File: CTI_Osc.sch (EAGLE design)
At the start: 15 parts, among them IC6 7805DT

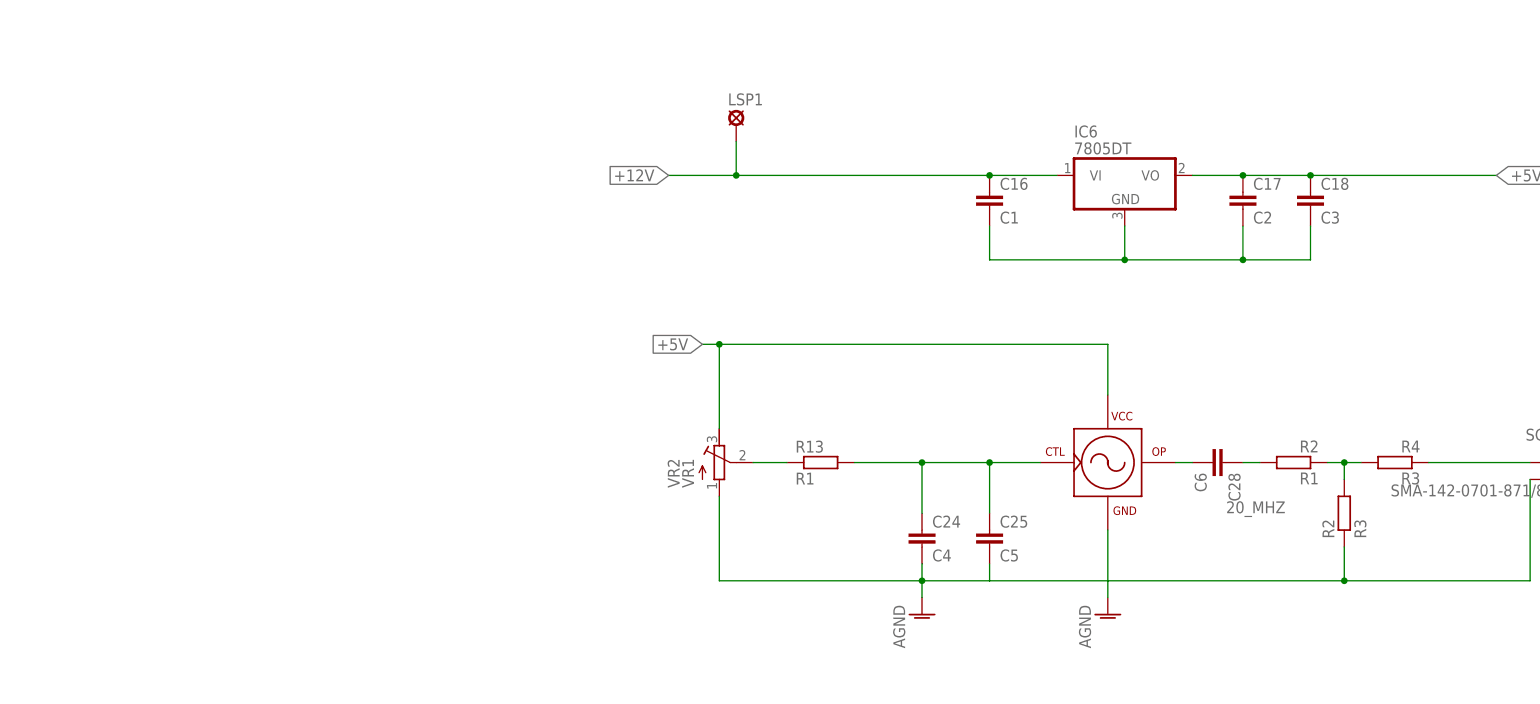
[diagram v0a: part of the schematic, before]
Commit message: V1 release
Added a TL431C for precision control of the freq set pin.
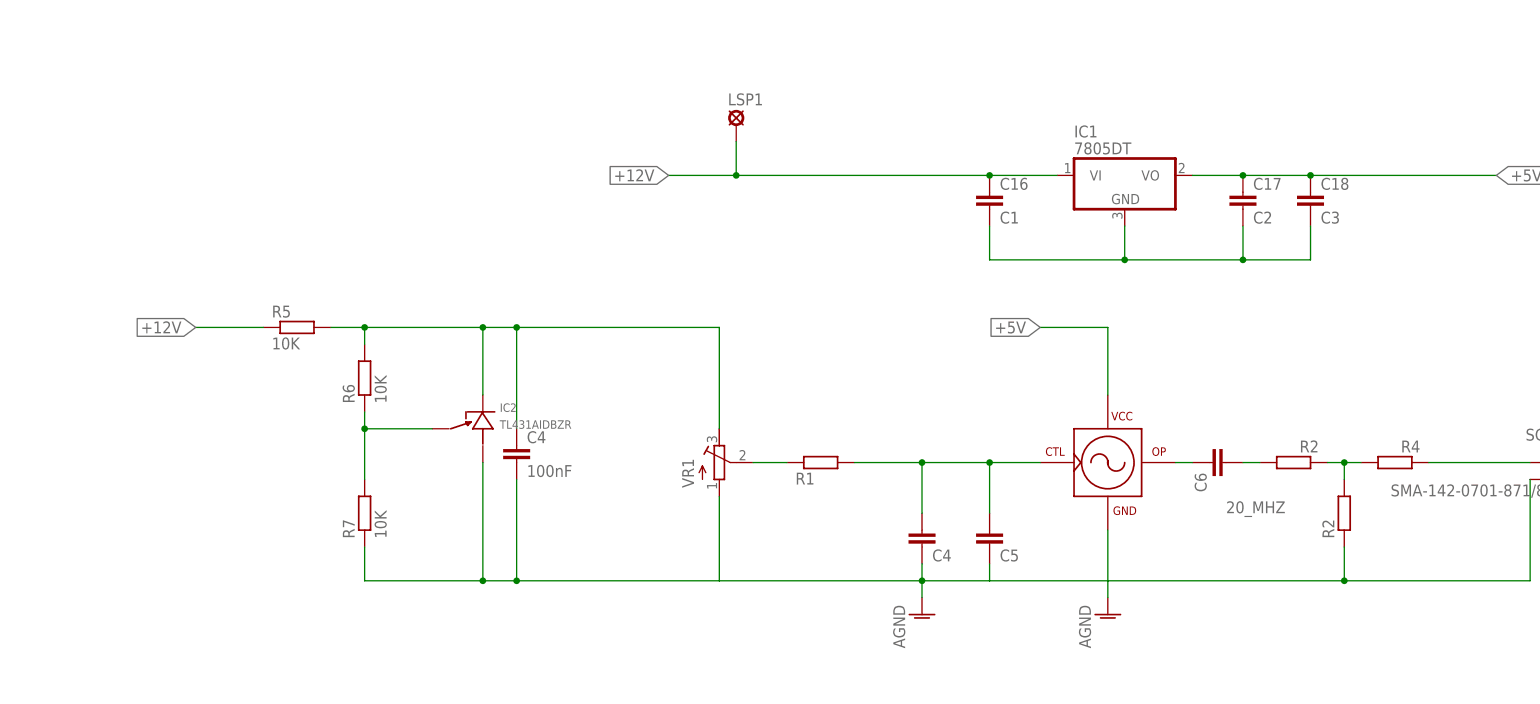
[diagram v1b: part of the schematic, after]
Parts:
- added C4: 100nF, rcl:C-EUC0603
- added IC2: TL431AIDBZR, RF:TL431AIDBZR
- added R5, R6, R7: 10K, rcl:R-EU_R0603
- renumbered IC6 to IC1
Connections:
- new net +5V_PRECISION: C4.1, IC2.CATHODE, R5.2, R6.2, VR2.A
- new net N$42: IC2.CTRL, R6.1, R7.2
- net +12V: now also R5.1
- net +5V: no longer VR2.A
- net GND: now also C4.2, IC2.ANODE, R7.1
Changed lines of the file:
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@@
 <part name="SCK1" library="con-coax" deviceset="SMA-" device="142-0701-871/876"/>
 <part name="OSC1" library="RF" deviceset="CTI_OSC" device=""/>
-<part name="IC6" library="linear" deviceset="78*" device="DT" technology="05" value="7805DT"/>
+<part name="IC1" library="linear" deviceset="78*" device="DT" technology="05" value="7805DT"/>
 <part name="C16" library="rcl" deviceset="C-EU" device="C0805" value="C1"/>
 <part name="C17" library="rcl" deviceset="C-EU" device="C0805" value="C2"/>
@@
 <part name="R1" library="rcl" deviceset="R-EU_" device="R0603" value="R2"/>
 <part name="VR2" library="resistor" deviceset="R-TRIMM" device="64Y" value="VR1"/>
+<part name="IC2" library="RF" deviceset="TL431AIDBZR" device=""/>
+<part name="R5" library="rcl" deviceset="R-EU_" device="R0603" value="10K"/>
+<part name="R7" library="rcl" deviceset="R-EU_" device="R0603" value="10K"/>
+<part name="R6" library="rcl" deviceset="R-EU_" device="R0603" value="10K"/>
+<part name="C4" library="rcl" deviceset="C-EU" device="C0603" value="100nF"/>
 </parts>
 <sheets>
@@
 <instance part="U$5" gate="CCSA" x="515.62" y="0"/>
 <instance part="AGND39" gate="VR1" x="175.26" y="152.4"/>
-<instance part="C24" gate="G$1" x="147.32" y="165.1"/>
+<instance part="C24" gate="G$1" x="147.32" y="165.1" smashed="yes">
+<attribute name="VALUE" x="148.844" y="160.401" size="1.778" layer="96"/>
+</instance>
 <instance part="AGND40" gate="VR1" x="147.32" y="152.4"/>
-<instance part="C25" gate="G$1" x="157.48" y="165.1"/>
-<instance part="R13" gate="G$1" x="132.08" y="175.26"/>
-<instance part="C28" gate="G$1" x="193.04" y="175.26" rot="R270"/>
+<instance part="C25" gate="G$1" x="157.48" y="165.1" smashed="yes">
+<attribute name="VALUE" x="159.004" y="160.401" size="1.778" layer="96"/>
+</instance>
+<instance part="R13" gate="G$1" x="132.08" y="175.26" smashed="yes">
+<attribute name="VALUE" x="128.27" y="171.958" size="1.778" layer="96"/>
+</instance>
+<instance part="C28" gate="G$1" x="193.04" y="175.26" smashed="yes" rot="R270">
+<attribute name="VALUE" x="188.341" y="173.736" size="1.778" layer="96" rot="R270"/>
+</instance>
 <instance part="SCK1" gate="G1" x="241.3" y="175.26" rot="MR0"/>
 <instance part="OSC1" gate="G$1" x="170.18" y="170.18"/>
-<instance part="IC6" gate="A1" x="177.8" y="218.44"/>
+<instance part="IC1" gate="A1" x="177.8" y="218.44"/>
 <instance part="C16" gate="G$1" x="157.48" y="215.9"/>
 <instance part="C17" gate="G$1" x="195.58" y="215.9"/>
 <instance part="C18" gate="G$1" x="205.74" y="215.9"/>
 <instance part="LSP1" gate="1" x="119.38" y="226.06"/>
-<instance part="R2" gate="G$1" x="210.82" y="167.64" rot="R90"/>
-<instance part="R3" gate="G$1" x="218.44" y="175.26" rot="R180"/>
-<instance part="R1" gate="G$1" x="203.2" y="175.26" rot="R180"/>
-<instance part="VR2" gate="G$1" x="116.84" y="175.26"/>
+<instance part="R2" gate="G$1" x="210.82" y="167.64" smashed="yes" rot="R90">
+<attribute name="NAME" x="209.3214" y="163.83" size="1.778" layer="95" rot="R90"/>
+</instance>
+<instance part="R3" gate="G$1" x="218.44" y="175.26" smashed="yes" rot="R180">
+<attribute name="VALUE" x="222.25" y="178.562" size="1.778" layer="96" rot="R180"/>
+</instance>
+<instance part="R1" gate="G$1" x="203.2" y="175.26" smashed="yes" rot="R180">
+<attribute name="VALUE" x="207.01" y="178.562" size="1.778" layer="96" rot="R180"/>
+</instance>
+<instance part="VR2" gate="G$1" x="116.84" y="175.26" smashed="yes">
+<attribute name="VALUE" x="113.03" y="171.45" size="1.778" layer="96" rot="R90"/>
+</instance>
+<instance part="IC2" gate="G$1" x="81.28" y="180.34"/>
+<instance part="R5" gate="G$1" x="53.34" y="195.58"/>
+<instance part="R7" gate="G$1" x="63.5" y="167.64" rot="R90"/>
+<instance part="R6" gate="G$1" x="63.5" y="187.96" rot="R90"/>
+<instance part="C4" gate="G$1" x="86.36" y="177.8"/>
 </instances>
 <busses>
@@
 <pinref part="C16" gate="G$1" pin="2"/>
 <wire x1="157.48" y1="210.82" x2="157.48" y2="205.74" width="0.1524" layer="91"/>
-<pinref part="IC6" gate="A1" pin="GND"/>
+<pinref part="IC1" gate="A1" pin="GND"/>
 <wire x1="157.48" y1="205.74" x2="177.8" y2="205.74" width="0.1524" layer="91"/>
 <wire x1="177.8" y1="205.74" x2="177.8" y2="210.82" width="0.1524" layer="91"/>
@@
 <junction x="210.82" y="157.48"/>
 <pinref part="VR2" gate="G$1" pin="E"/>
+<pinref part="IC2" gate="G$1" pin="ANODE"/>
+<wire x1="81.28" y1="175.26" x2="81.28" y2="157.48" width="0.1524" layer="91"/>
+<wire x1="81.28" y1="157.48" x2="86.36" y2="157.48" width="0.1524" layer="91"/>
+<pinref part="R7" gate="G$1" pin="1"/>
+<wire x1="86.36" y1="157.48" x2="116.84" y2="157.48" width="0.1524" layer="91"/>
+<wire x1="63.5" y1="162.56" x2="63.5" y2="157.48" width="0.1524" layer="91"/>
+<wire x1="63.5" y1="157.48" x2="81.28" y2="157.48" width="0.1524" layer="91"/>
+<junction x="81.28" y="157.48"/>
+<pinref part="C4" gate="G$1" pin="2"/>
+<wire x1="86.36" y1="172.72" x2="86.36" y2="157.48" width="0.1524" layer="91"/>
+<junction x="86.36" y="157.48"/>
 </segment>
 </net>
@@
 <wire x1="119.38" y1="218.44" x2="109.22" y2="218.44" width="0.1524" layer="91"/>
 <pinref part="C16" gate="G$1" pin="1"/>
-<pinref part="IC6" gate="A1" pin="VI"/>
+<pinref part="IC1" gate="A1" pin="VI"/>
 <wire x1="157.48" y1="218.44" x2="167.64" y2="218.44" width="0.1524" layer="91"/>
 <junction x="157.48" y="218.44"/>
@@
 <wire x1="119.38" y1="223.52" x2="119.38" y2="218.44" width="0.1524" layer="91"/>
 <junction x="119.38" y="218.44"/>
+</segment>
+<segment>
+<pinref part="R5" gate="G$1" pin="1"/>
+<wire x1="48.26" y1="195.58" x2="38.1" y2="195.58" width="0.1524" layer="91"/>
+<label x="38.1" y="195.58" size="1.778" layer="95" rot="R180" xref="yes"/>
 </segment>
 </net>
@@
 <net name="+5V" class="0">
 <segment>
-<wire x1="116.84" y1="193.04" x2="175.26" y2="193.04" width="0.1524" layer="91"/>
-<wire x1="175.26" y1="193.04" x2="175.26" y2="185.42" width="0.1524" layer="91"/>
-<label x="114.3" y="193.04" size="1.778" layer="95" rot="R180" xref="yes"/>
-<wire x1="116.84" y1="193.04" x2="114.3" y2="193.04" width="0.1524" layer="91"/>
-<wire x1="116.84" y1="180.34" x2="116.84" y2="193.04" width="0.1524" layer="91"/>
-<junction x="116.84" y="193.04"/>
-<pinref part="OSC1" gate="G$1" pin="VCC"/>
-<pinref part="VR2" gate="G$1" pin="A"/>
-</segment>
-<segment>
-<pinref part="IC6" gate="A1" pin="VO"/>
+<pinref part="IC1" gate="A1" pin="VO"/>
 <pinref part="C17" gate="G$1" pin="1"/>
 <wire x1="187.96" y1="218.44" x2="195.58" y2="218.44" width="0.1524" layer="91"/>
@@
 <label x="233.68" y="218.44" size="1.778" layer="95" xref="yes"/>
 </segment>
+<segment>
+<wire x1="175.26" y1="195.58" x2="175.26" y2="185.42" width="0.1524" layer="91"/>
+<pinref part="OSC1" gate="G$1" pin="VCC"/>
+<wire x1="165.1" y1="195.58" x2="175.26" y2="195.58" width="0.1524" layer="91"/>
+<label x="165.1" y="195.58" size="1.778" layer="95" rot="R180" xref="yes"/>
+</segment>
 </net>
 <net name="20_MHZ" class="0">
@@
 </segment>
 </net>
+<net name="+5V_PRECISION" class="0">
+<segment>
+<pinref part="IC2" gate="G$1" pin="CATHODE"/>
+<wire x1="81.28" y1="185.42" x2="81.28" y2="195.58" width="0.1524" layer="91"/>
+<wire x1="81.28" y1="195.58" x2="86.36" y2="195.58" width="0.1524" layer="91"/>
+<pinref part="R5" gate="G$1" pin="2"/>
+<wire x1="86.36" y1="195.58" x2="116.84" y2="195.58" width="0.1524" layer="91"/>
+<wire x1="58.42" y1="195.58" x2="63.5" y2="195.58" width="0.1524" layer="91"/>
+<wire x1="63.5" y1="195.58" x2="81.28" y2="195.58" width="0.1524" layer="91"/>
+<pinref part="R6" gate="G$1" pin="2"/>
+<wire x1="63.5" y1="193.04" x2="63.5" y2="195.58" width="0.1524" layer="91"/>
+<junction x="63.5" y="195.58"/>
+<junction x="81.28" y="195.58"/>
+<pinref part="C4" gate="G$1" pin="1"/>
+<wire x1="86.36" y1="180.34" x2="86.36" y2="195.58" width="0.1524" layer="91"/>
+<junction x="86.36" y="195.58"/>
+<wire x1="116.84" y1="180.34" x2="116.84" y2="195.58" width="0.1524" layer="91"/>
+<pinref part="VR2" gate="G$1" pin="A"/>
+</segment>
+</net>
+<net name="N$42" class="0">
+<segment>
+<pinref part="R6" gate="G$1" pin="1"/>
+<wire x1="63.5" y1="182.88" x2="63.5" y2="180.34" width="0.1524" layer="91"/>
+<pinref part="IC2" gate="G$1" pin="CTRL"/>
+<wire x1="63.5" y1="180.34" x2="73.66" y2="180.34" width="0.1524" layer="91"/>
+<pinref part="R7" gate="G$1" pin="2"/>
+<wire x1="63.5" y1="172.72" x2="63.5" y2="180.34" width="0.1524" layer="91"/>
+<junction x="63.5" y="180.34"/>
+</segment>
+</net>
